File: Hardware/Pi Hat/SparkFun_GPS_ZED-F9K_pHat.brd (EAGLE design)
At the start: 65 x 57.3 mm, 121 parts, among them J1 QWIIC_RIGHT_ANGLE, J2 RASPBERRYPI-40-PIN-GPIO_SMD_S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, J4 U.FL, U1 UBLOX_ZED_F9R, U2 HCPL-270L

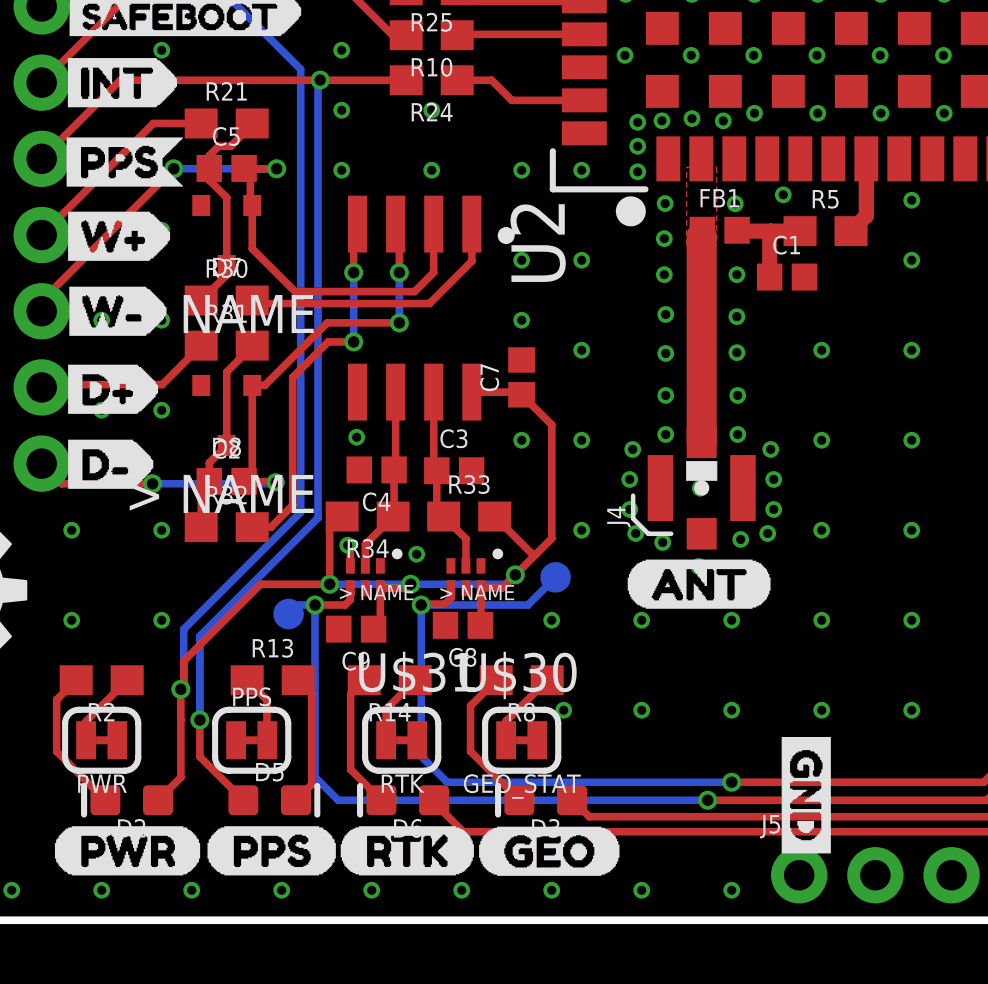
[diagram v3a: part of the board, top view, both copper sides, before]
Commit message: Removes gerbers, removes caps from schmitt trigger on both designs, adds 1uF cap to V_USB on breakout
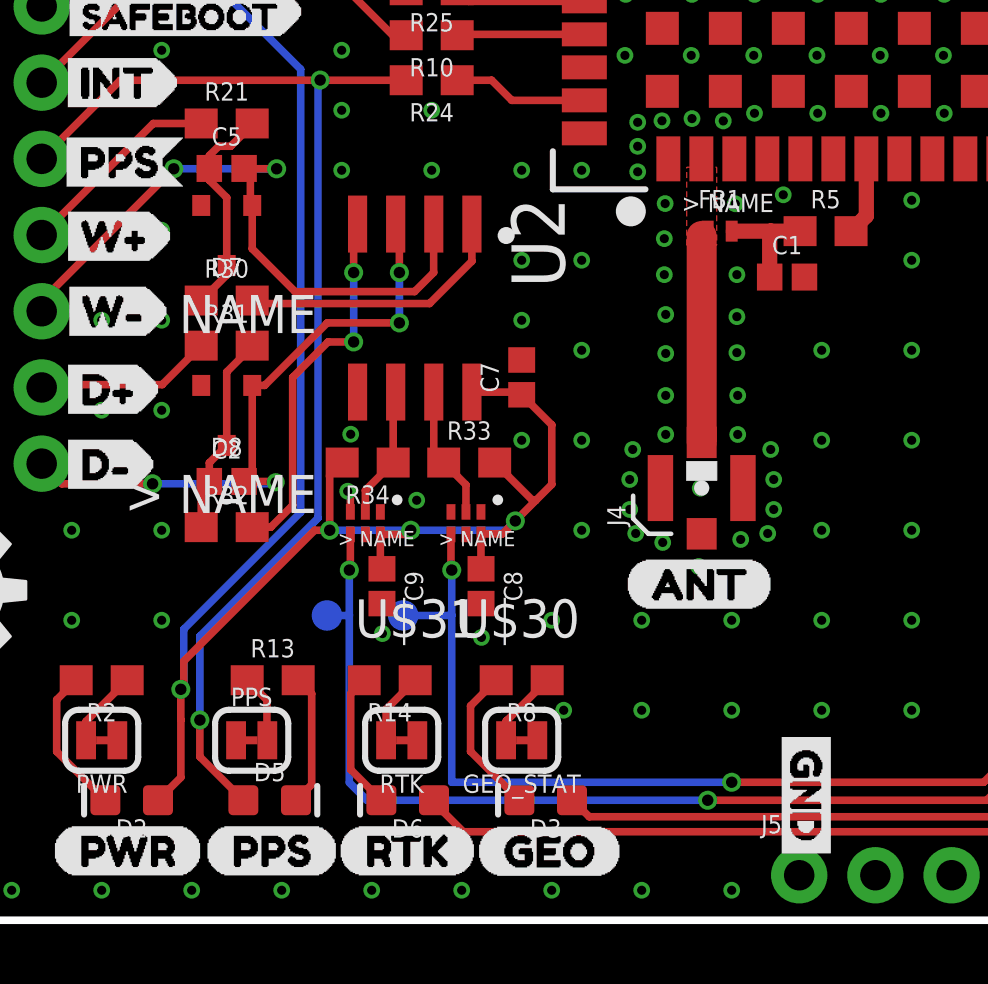
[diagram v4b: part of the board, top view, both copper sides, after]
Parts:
- removed C3, C4: 22nF, SparkFun-Capacitors:0402
- FB1: value FERRITE_BEAD-120_OHM-0402 -> 120NH; device SparkFun-Coils:0402 -> SparkFun-Coils:0402_MURATA
- R5: value 10 -> 33
- moved TP6 5.24 mm to (19.1, 10.2)
- moved U$30 1.80 mm to (21.1, 13.2)
- moved U$31 1.80 mm to (17.8, 13.2)
- moved R33 1.80 mm to (21.2, 15.3)
- moved R34 1.80 mm to (17.9, 15.3)
- moved C9 1.67 mm to (18.3, 11.1), turned to 270 degrees
- moved C8 1.44 mm to (21.6, 11.1), turned to 270 degrees
- moved TP7 1.28 mm to (16.5, 10.2)
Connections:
- net DIR_SCHMITT: no longer C4.1
- net GND: no longer C3.2, C4.2
- net N$5: now also FB1.P2; no longer FB1.2
- net RF_IN: now also FB1.P1; no longer FB1.1
- net WT_SCHMITT: no longer C3.1
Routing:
- net WT_OUT: track 69.9 -> 67.1 mm
- net WT_SCHMITT: track 6.24 -> 4.44 mm
- net DIR_SCHMITT: track 6.21 -> 4.46 mm
- net 3.3V: track 152.9 -> 151.5 mm
- net DIR_OUT: track 73.5 -> 72.9 mm
- net GND: vias 299 -> 301

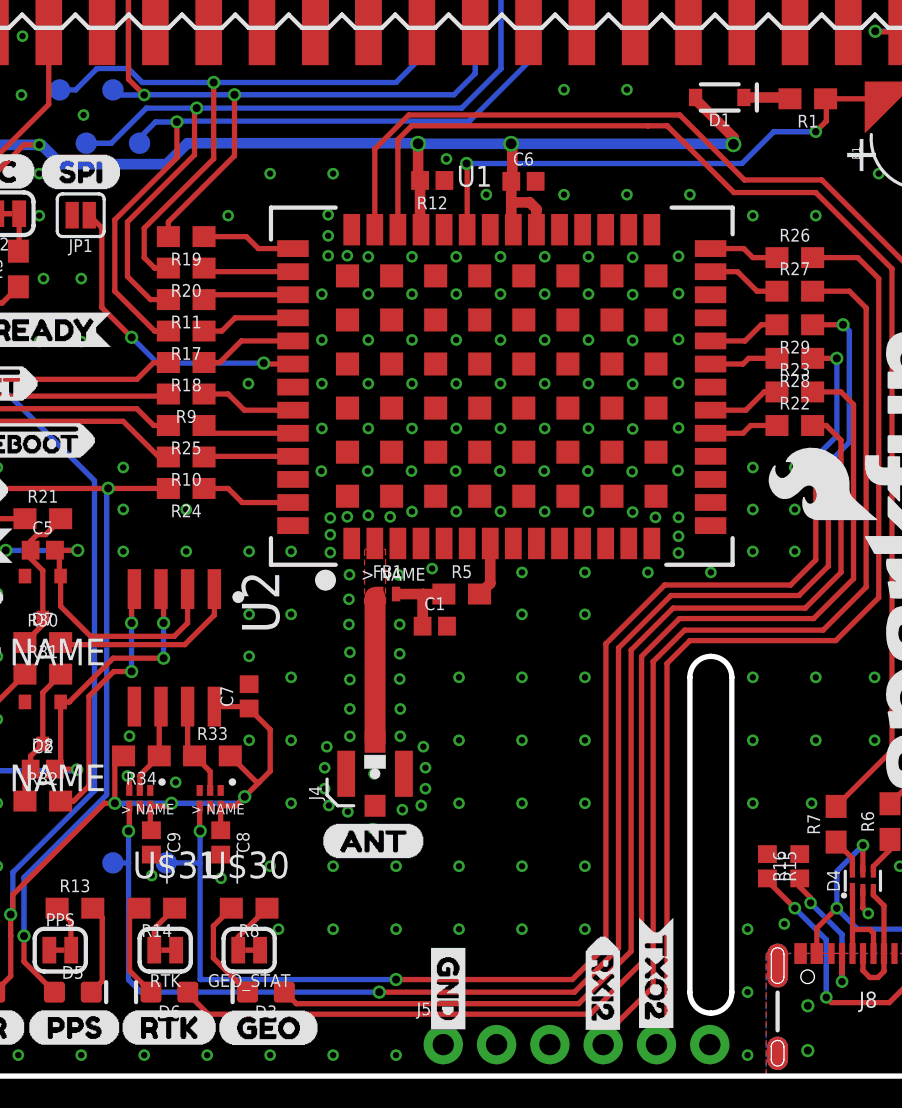
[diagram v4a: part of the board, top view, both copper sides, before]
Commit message: Adds 1uF Cap to V_USB line
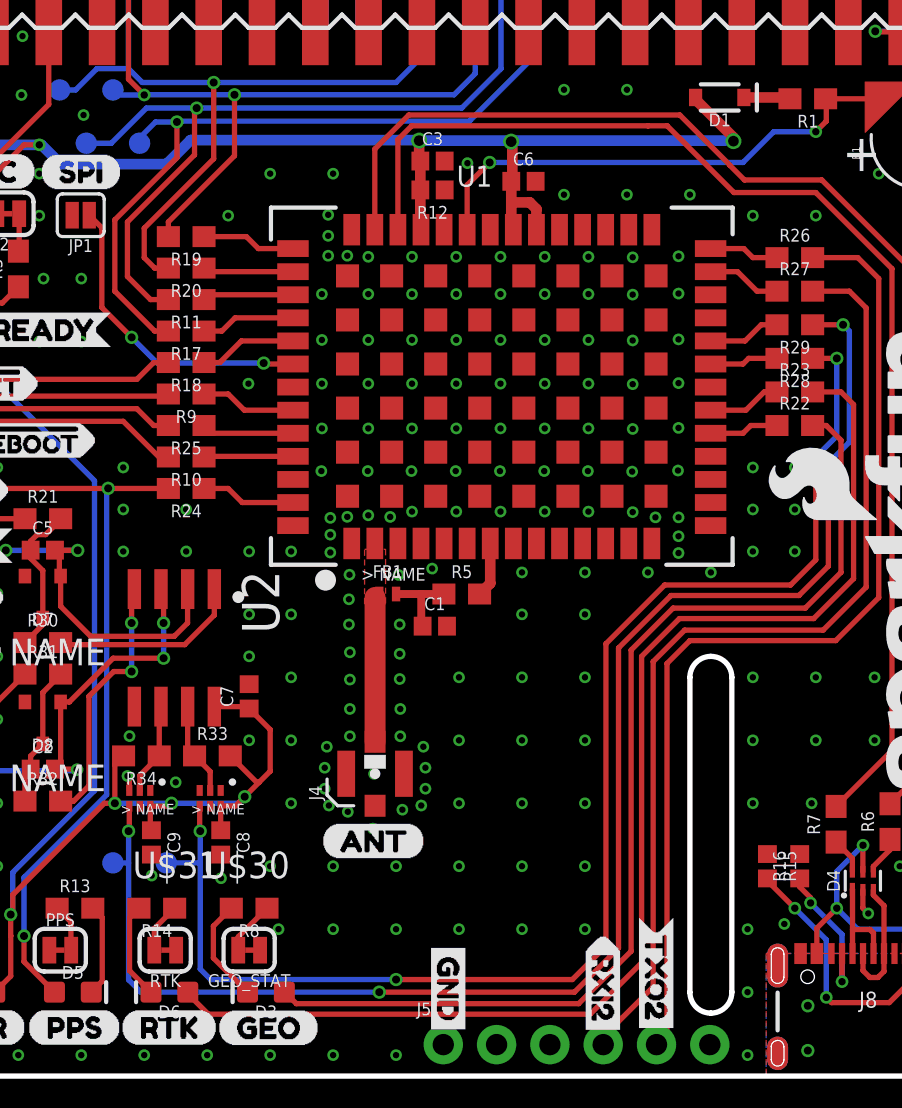
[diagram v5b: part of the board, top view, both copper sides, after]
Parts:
- added C3: 1.0uF, SparkFun-Capacitors:0402
- moved R12 0.45 mm to (31.7, 42.2)
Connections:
- net 3.3V: now also C3.1
- net GND: now also C3.2
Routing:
- net V_BATT: track 24.8 -> 24.2 mm
- net GND: vias 301 -> 300

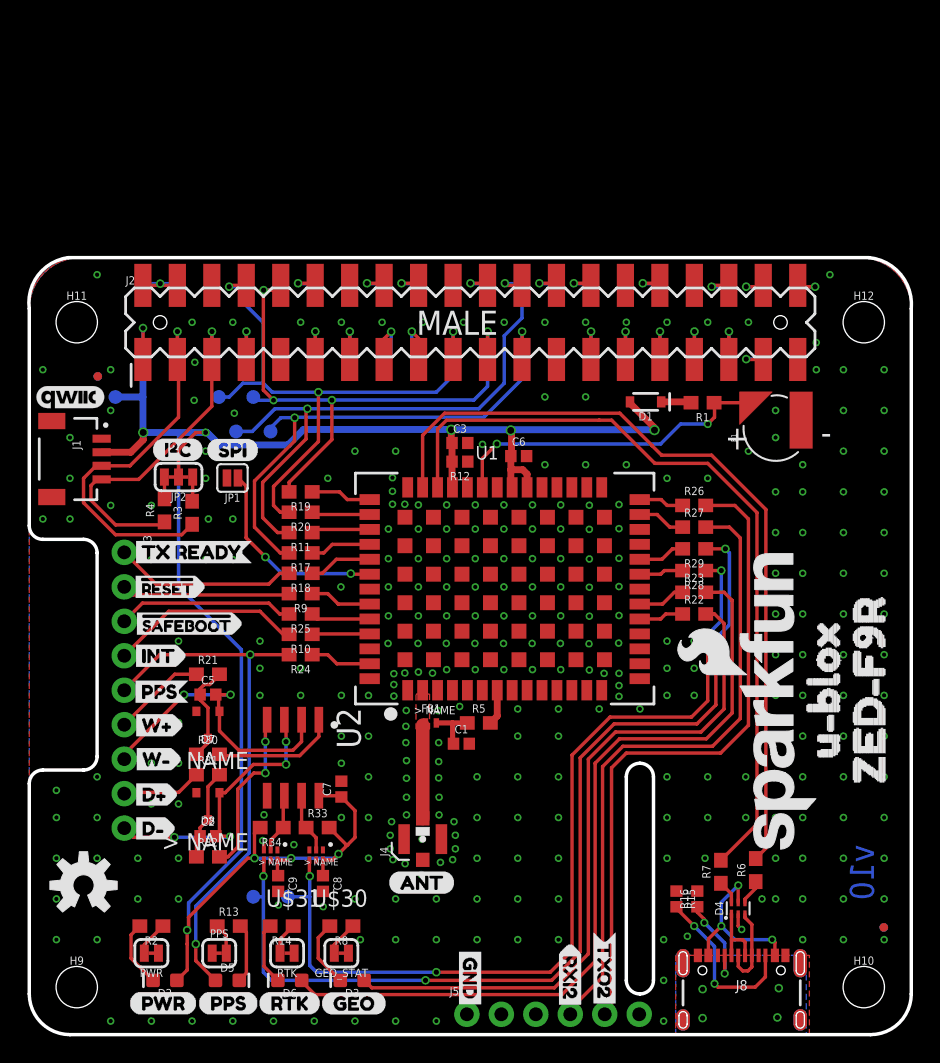
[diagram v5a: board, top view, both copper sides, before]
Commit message: Updates wheel tick and direction circuitry with correct grounding
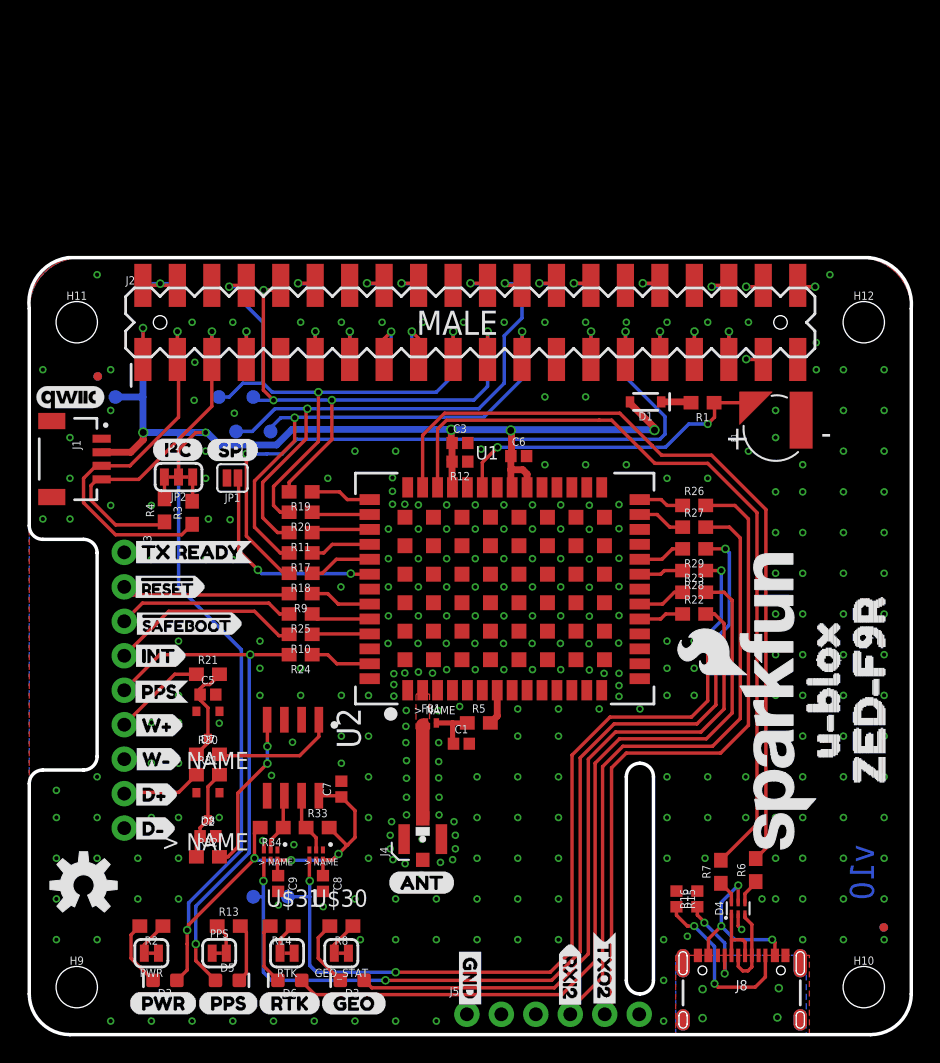
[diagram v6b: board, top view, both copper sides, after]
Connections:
- removed net DIR-: C2.2, D8.P1, J3.9, U2.P3
- removed net GP5: J2.29, J2.29B
- removed net WT-: C5.2, D7.P1, J3.7, U2.P2
- net GND: now also C2.2, C5.2, D7.P1, D8.P1, J3.7, J3.9, U2.P2, U2.P3
- net TX_READY: now also J2.29, J2.29B; no longer J3.1
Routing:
- net TX_READY: track 13.5 -> 52.6 mm, vias 0 -> 2
- net WT-: track 22.4 -> 0.00 mm, vias 2 -> 0
- net DIR-: track 21.6 -> 0.00 mm, vias 4 -> 0
- net GP5: track 4.23 -> 0.00 mm, vias 1 -> 0
- net D_SEL: track 14.9 -> 15.7 mm
- net GND: track 1.96 -> 2.13 mm, vias 300 -> 304
